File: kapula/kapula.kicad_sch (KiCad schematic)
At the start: 167 parts, among them J1 Conn_02x10_Odd_Even, J12 U.FL, J13 U.FL, J3 Conn_02x10_Odd_Even, J4 Conn_ARM_JTAG_SWD_10, J5 U.FL, J9 U.FL, Q1 AO3401A, Q1 BSS84, Q2 AO3401A, Q3 AO3400A, Q5 AO3400A, Q6 AO3400A, T1 BW21S7511A01TF, T2 BW21S7511A01TF, T3 BW21S7511A01TF, T4 BW21S7511A01TF, U1 XC6206P332MR, U2 TP4054, U3 DW01+G, U5 EFR32FG14P233F256GM48-B, U6 XA213-G4J, X1 DSB221SDN, Y1 32768 Hz

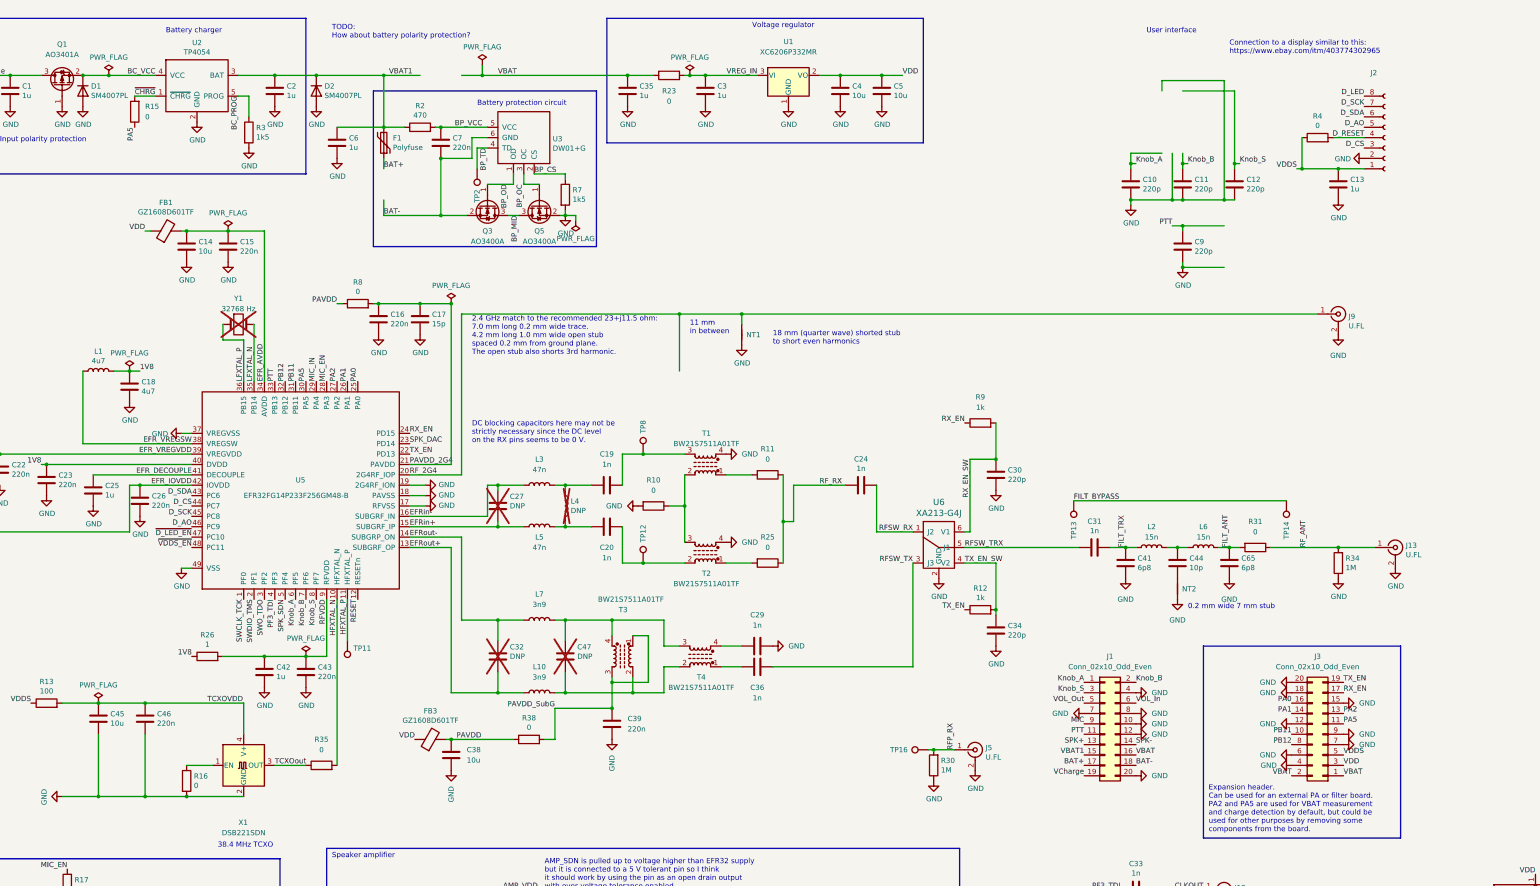
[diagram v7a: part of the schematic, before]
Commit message: PCB: Change some components, fix some DRC issues
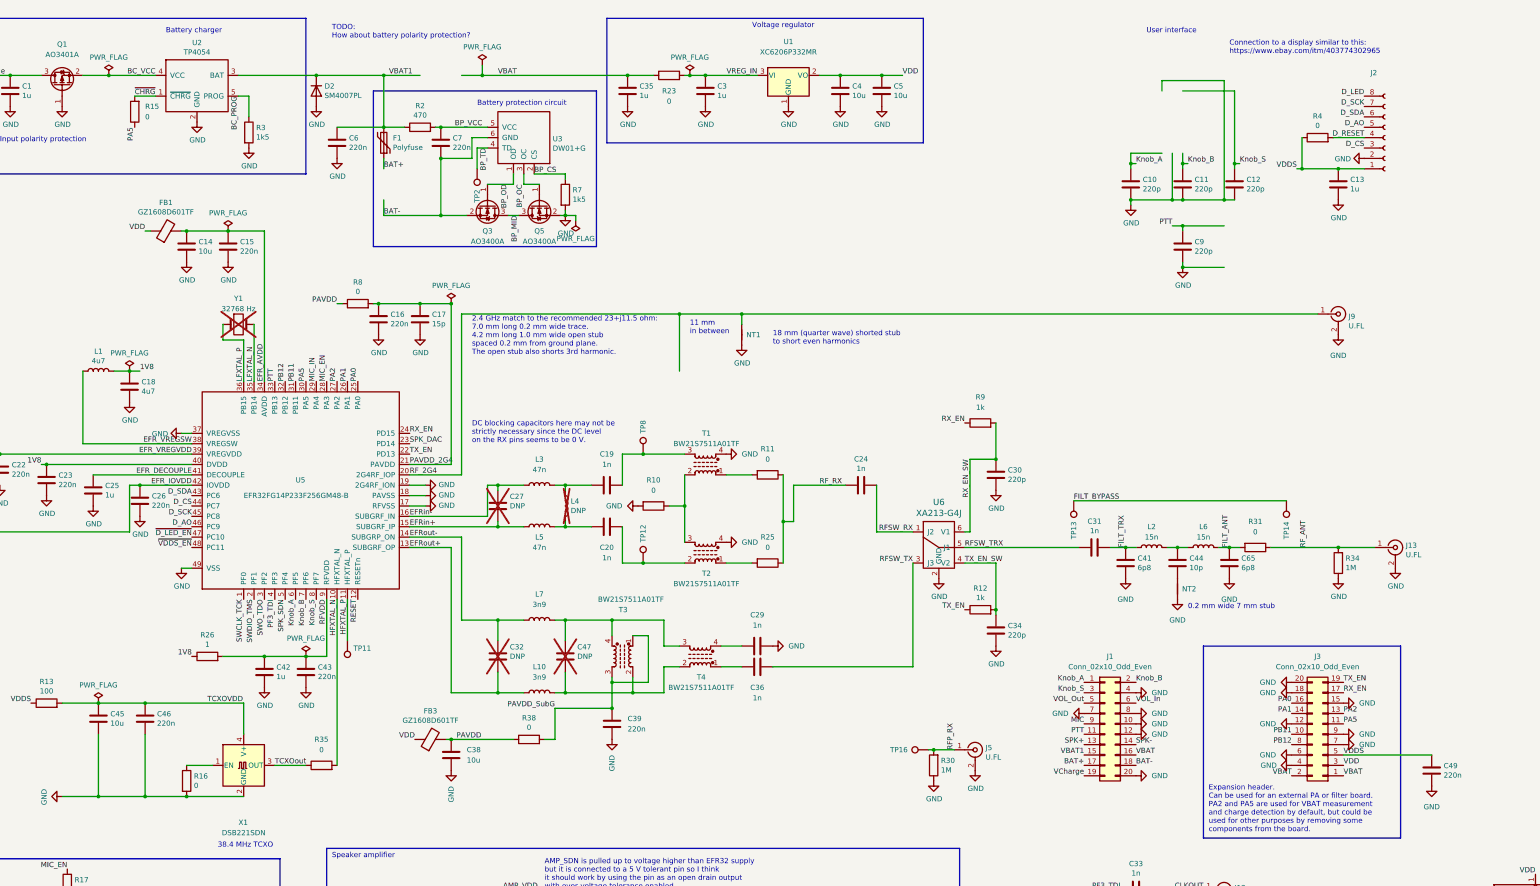
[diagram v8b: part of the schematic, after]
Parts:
- removed C2: 1u, Capacitor_SMD:C_0603_1608Metric, symbol Device:C
- removed D1: SM4007PL, Diode_SMD:D_SOD-123F, symbol Device:D
- added C49: 220n, Capacitor_SMD:C_0402_1005Metric, symbol Device:C
- C6: value 1u -> 220n; footprint Capacitor_SMD:C_0603_1608Metric -> Capacitor_SMD:C_0402_1005Metric; LCSC C15849 -> C16772
- TP11, TP2: footprint TestPoint:TestPoint_Pad_D1.0mm -> kapula:Pad_1mm
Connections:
- net GND: now also C49.2
- net VDDS: now also C49.1
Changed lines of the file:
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@@
   (junction (at 377.19 -21.59) (diameter 0) (color 0 0 0 0)
   )
-  (junction (at 130.81 26.67) (diameter 0) (color 0 0 0 0)
-  )
   (junction (at 156.21 82.55) (diameter 0) (color 0 0 0 0)
   )
@@
   (junction (at 198.12 -21.59) (diameter 0) (color 0 0 0 0)
   )
-  (junction (at 83.82 26.67) (diameter 0) (color 0 0 0 0)
-  )
   (junction (at 138.43 168.91) (diameter 0) (color 0 0 0 0)
   )
@@
     (stroke (width 0) (type default))
   )
+  (wire (pts (xy 392.43 193.04) (xy 414.02 193.04))
+    (stroke (width 0) (type default))
+  )
   (wire (pts (xy 236.22 26.67) (xy 248.92 26.67))
     (stroke (width 0) (type default))
@@
     (stroke (width 0) (type default))
   )
-  (wire (pts (xy 130.81 26.67) (xy 140.97 26.67))
-    (stroke (width 0) (type default))
-  )
   (wire (pts (xy 219.71 261.62) (xy 226.06 261.62))
     (stroke (width 0) (type default))
@@
     (stroke (width 0) (type default))
   )
-  (wire (pts (xy 121.92 26.67) (xy 130.81 26.67))
+  (wire (pts (xy 121.92 26.67) (xy 140.97 26.67))
     (stroke (width 0) (type default))
   )
@@
     )
   )
-  (symbol (lib_id "Device:C") (at 130.81 30.48 0) (unit 1)
-    (in_bom yes) (on_board yes) (dnp no)
-    (property "Reference" "C2" (at 133.731 29.3116 0)
-      (effects (font (size 1.27 1.27)) (justify left))
-    )
-    (property "Value" "1u" (at 133.731 31.623 0)
-      (effects (font (size 1.27 1.27)) (justify left))
-    )
-    (property "Footprint" "Capacitor_SMD:C_0603_1608Metric" (at 131.7752 34.29 0)
-      (effects (font (size 1.27 1.27)) hide)
-    )
-    (property "Datasheet" "https://weblib.samsungsem.com/mlcc/mlcc-ec-data-sheet.do?partNumber=CL10A105KB8NNN" (at 130.81 30.48 0)
-      (effects (font (size 1.27 1.27)) hide)
-    )
-    (property "LCSC" "C15849" (at 130.81 30.48 0)
-      (effects (font (size 1.27 1.27)) hide)
-    )
-    (pin "1")
-    (pin "2")
-    (instances
-      (project "kapula"
-        (path "/f2315993-072e-45c9-8c85-e79c6d40aba4"
-          (reference "C2") (unit 1)
-        )
-      )
-    )
-  )
-  (symbol (lib_id "power:GND") (at 130.81 34.29 0) (unit 1)
-    (in_bom yes) (on_board yes) (dnp no)
-    (property "Reference" "#PWR05" (at 130.81 40.64 0)
-      (effects (font (size 1.27 1.27)) hide)
-    )
-    (property "Value" "GND" (at 130.937 38.6842 0)
-      (effects (font (size 1.27 1.27)))
-    )
-    (property "Footprint" "" (at 130.81 34.29 0)
-      (effects (font (size 1.27 1.27)) hide)
-    )
-    (property "Datasheet" "" (at 130.81 34.29 0)
-      (effects (font (size 1.27 1.27)) hide)
-    )
-    (pin "1")
-    (instances
-      (project "kapula"
-        (path "/f2315993-072e-45c9-8c85-e79c6d40aba4"
-          (reference "#PWR05") (unit 1)
-        )
-      )
-    )
-  )
   (symbol (lib_id "Device:C") (at 66.04 30.48 0) (unit 1)
     (in_bom yes) (on_board yes) (dnp no)
@@
       (effects (font (size 1.27 1.27)) (justify left))
     )
-    (property "Value" "1u" (at 148.971 44.323 0)
+    (property "Value" "220n" (at 148.971 44.323 0)
       (effects (font (size 1.27 1.27)) (justify left))
     )
-    (property "Footprint" "Capacitor_SMD:C_0603_1608Metric" (at 147.0152 46.99 0)
+    (property "Footprint" "Capacitor_SMD:C_0402_1005Metric" (at 147.0152 46.99 0)
       (effects (font (size 1.27 1.27)) hide)
     )
-    (property "Datasheet" "https://weblib.samsungsem.com/mlcc/mlcc-ec-data-sheet.do?partNumber=CL10A105KB8NNN" (at 146.05 43.18 0)
+    (property "Datasheet" "https://weblib.samsungsem.com/mlcc/mlcc-ec-data-sheet.do?partNumber=CL05B224KO5NNN" (at 146.05 43.18 0)
       (effects (font (size 1.27 1.27)) hide)
     )
-    (property "LCSC" "C15849" (at 146.05 43.18 0)
+    (property "LCSC" "C16772" (at 146.05 43.18 0)
       (effects (font (size 1.27 1.27)) hide)
     )
@@
     )
   )
-  (symbol (lib_id "Device:D") (at 83.82 30.48 270) (unit 1)
-    (in_bom yes) (on_board yes) (dnp no)
-    (property "Reference" "D1" (at 85.8266 29.3116 90)
-      (effects (font (size 1.27 1.27)) (justify left))
-    )
-    (property "Value" "SM4007PL" (at 85.8266 31.623 90)
-      (effects (font (size 1.27 1.27)) (justify left))
-    )
-    (property "Footprint" "Diode_SMD:D_SOD-123F" (at 83.82 30.48 0)
-      (effects (font (size 1.27 1.27)) hide)
-    )
-    (property "Datasheet" "https://datasheet.lcsc.com/szlcsc/1903051030_MDD-Jiangsu-Yutai-Elec-SM4007PL_C64898.pdf" (at 83.82 30.48 0)
-      (effects (font (size 1.27 1.27)) hide)
-    )
-    (property "LCSC" "C64898" (at 83.82 30.48 90)
-      (effects (font (size 1.27 1.27)) hide)
-    )
-    (property "Sim.Device" "D" (at 83.82 30.48 0)
-      (effects (font (size 1.27 1.27)) hide)
-    )
-    (property "Sim.Pins" "1=K 2=A" (at 83.82 30.48 0)
-      (effects (font (size 1.27 1.27)) hide)
-    )
-    (pin "1")
-    (pin "2")
-    (instances
-      (project "kapula"
-        (path "/f2315993-072e-45c9-8c85-e79c6d40aba4"
-          (reference "D1") (unit 1)
-        )
-      )
-    )
-  )
-  (symbol (lib_id "power:GND") (at 83.82 34.29 0) (unit 1)
-    (in_bom yes) (on_board yes) (dnp no)
-    (property "Reference" "#PWR04" (at 83.82 40.64 0)
-      (effects (font (size 1.27 1.27)) hide)
-    )
-    (property "Value" "GND" (at 83.947 38.6842 0)
-      (effects (font (size 1.27 1.27)))
-    )
-    (property "Footprint" "" (at 83.82 34.29 0)
-      (effects (font (size 1.27 1.27)) hide)
-    )
-    (property "Datasheet" "" (at 83.82 34.29 0)
-      (effects (font (size 1.27 1.27)) hide)
-    )
-    (pin "1")
-    (instances
-      (project "kapula"
-        (path "/f2315993-072e-45c9-8c85-e79c6d40aba4"
-          (reference "#PWR04") (unit 1)
-        )
-      )
-    )
-  )
   (symbol (lib_id "Connector:TestPoint") (at 180.34 49.53 180) (unit 1)
     (in_bom yes) (on_board yes) (dnp no)
@@
       (effects (font (size 1.27 1.27)) (justify right))
     )
-    (property "Footprint" "TestPoint:TestPoint_Pad_D1.0mm" (at 175.26 49.53 0)
+    (property "Footprint" "kapula:Pad_1mm" (at 175.26 49.53 0)
       (effects (font (size 1.27 1.27)) hide)
     )
@@
       (effects (font (size 1.27 1.27)) (justify right))
     )
-    (property "Footprint" "TestPoint:TestPoint_Pad_D1.0mm" (at 143.51 165.1 0)
+    (property "Footprint" "kapula:Pad_1mm" (at 143.51 165.1 0)
       (effects (font (size 1.27 1.27)) hide)
     )
@@
     )
   )
+  (symbol (lib_id "power:GND") (at 414.02 200.66 0) (unit 1)
+    (in_bom yes) (on_board yes) (dnp no) (fields_autoplaced)
+    (property "Reference" "#PWR083" (at 414.02 207.01 0)
+      (effects (font (size 1.27 1.27)) hide)
+    )
+    (property "Value" "GND" (at 414.02 205.74 0)
+      (effects (font (size 1.27 1.27)))
+    )
+    (property "Footprint" "" (at 414.02 200.66 0)
+      (effects (font (size 1.27 1.27)) hide)
+    )
+    (property "Datasheet" "" (at 414.02 200.66 0)
+      (effects (font (size 1.27 1.27)) hide)
+    )
+    (pin "1")
+    (instances
+      (project "kapula"
+        (path "/f2315993-072e-45c9-8c85-e79c6d40aba4"
+          (reference "#PWR083") (unit 1)
+        )
+      )
+    )
+  )
   (symbol (lib_id "Device:R") (at 251.46 146.05 270) (unit 1)
     (in_bom yes) (on_board yes) (dnp no) (fields_autoplaced)
@@
         )
       )
+    )
+  )
+  (symbol (lib_id "Device:C") (at 414.02 196.85 0) (unit 1)
+    (in_bom yes) (on_board yes) (dnp no)
+    (property "Reference" "C49" (at 416.941 195.6816 0)
+      (effects (font (size 1.27 1.27)) (justify left))
+    )
+    (property "Value" "220n" (at 416.941 197.993 0)
+      (effects (font (size 1.27 1.27)) (justify left))
+    )
+    (property "Footprint" "Capacitor_SMD:C_0402_1005Metric" (at 414.9852 200.66 0)
+      (effects (font (size 1.27 1.27)) hide)
+    )
+    (property "Datasheet" "https://weblib.samsungsem.com/mlcc/mlcc-ec-data-sheet.do?partNumber=CL05B224KO5NNN" (at 414.02 196.85 0)
+      (effects (font (size 1.27 1.27)) hide)
+    )
+    (property "LCSC" "C16772" (at 414.02 196.85 0)
+      (effects (font (size 1.27 1.27)) hide)
+    )
+    (pin "1")
+    (pin "2")
+    (instances
+      (project "kapula"
+        (path "/f2315993-072e-45c9-8c85-e79c6d40aba4"
+          (reference "C49") (unit 1)
+        )
+      )
